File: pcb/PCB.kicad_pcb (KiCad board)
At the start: 4 copper layers, 82.4 x 100 mm, 140 parts, among them J1 DTM1312PA12PBR008, J2 TC2030, J3 Conn_02x08_Top_Bottom, Q1 Si4162DY, Q2 Si4162DY, Q3 Si4162DY, Q4 Si4162DY, Q5 Si4162DY, Q6 Si4162DY, U1 SN65HVD230, U10 MCP1416, U11 BTS7004-1EPP, U12 BTS7004-1EPP, U13 BTS7004-1EPP, U14 BTS7004-1EPP, U15 BTS7004-1EPP, U2 AMS1117-3.3, U3 STM32F103C8T6, U4 BTS7004-1EPP, U5 MCP1416, U6 MCP1416, U7 MCP1416, U8 MCP1416, U9 MCP1416, Y1 8MHz

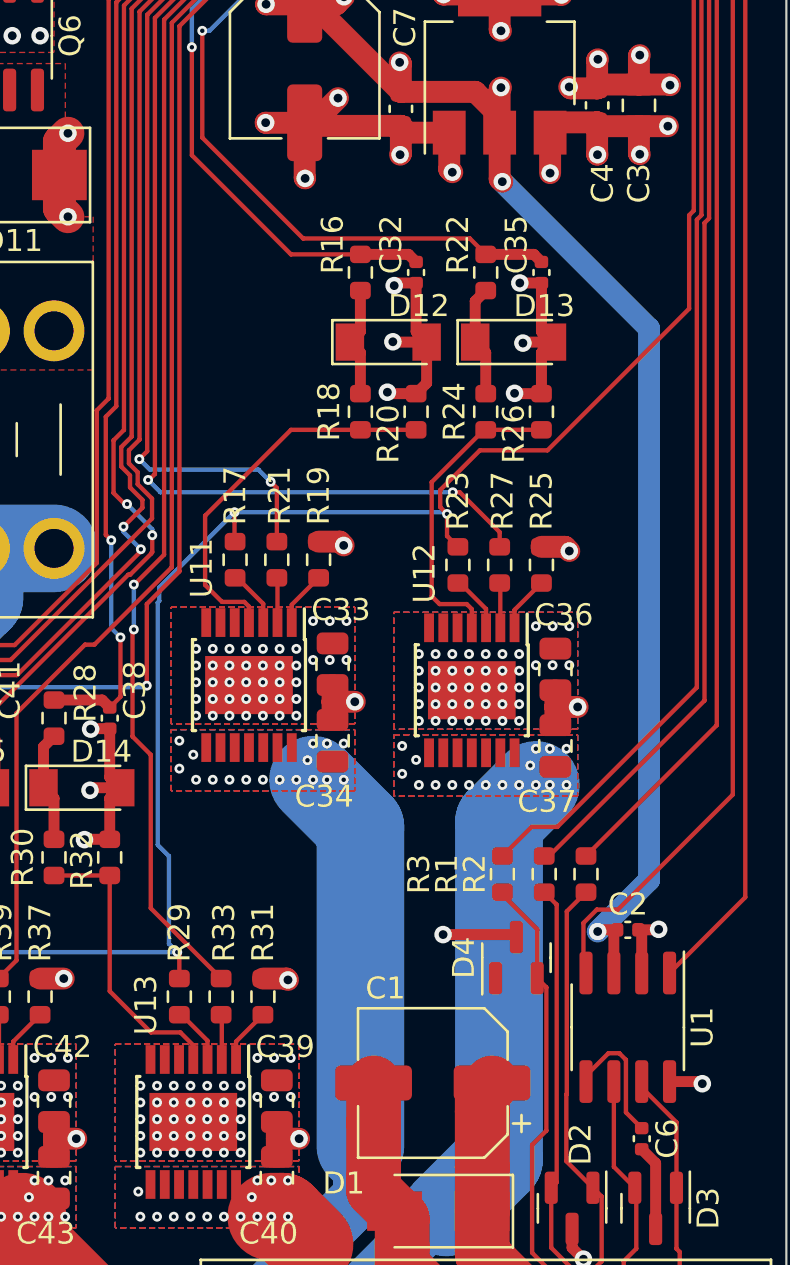
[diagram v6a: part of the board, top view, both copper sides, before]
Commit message: Added debug/test header
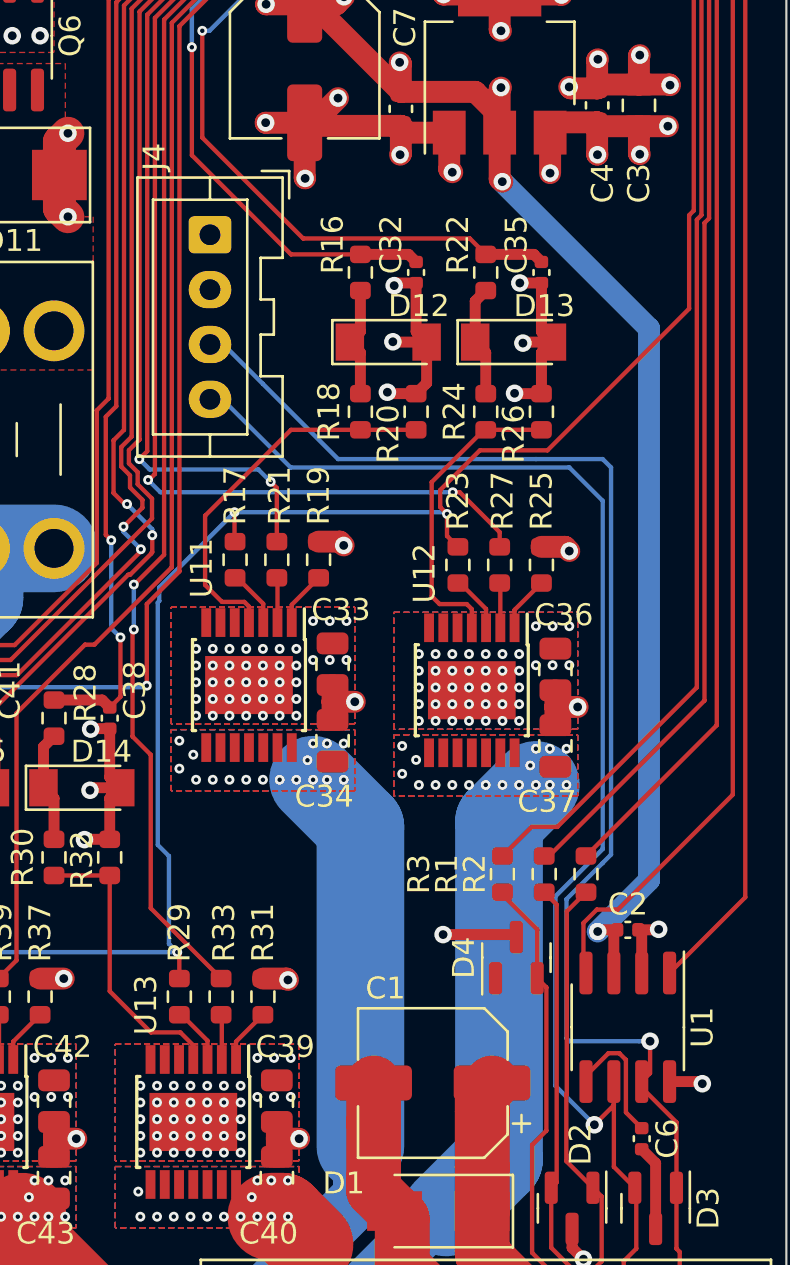
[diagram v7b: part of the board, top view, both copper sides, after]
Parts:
- added J4: JST B04B-XASK, Connector_JST:JST_XA_B04B-XASK-1_1x04_P2.50mm_Vertical, F.Cu at (124.0, 85.9)
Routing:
- net CAN+: track 11.3 -> 64.8 mm, vias 0 -> 1
- net CAN-: track 10.7 -> 63.2 mm, vias 0 -> 1
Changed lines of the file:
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@@
     )
   )
+  (footprint "Connector_JST:JST_XA_B04B-XASK-1_1x04_P2.50mm_Vertical" (layer "F.Cu")
+    (at 123.952 85.912 -90)
+    (descr "JST XA series connector, B04B-XASK-1 (http://www.jst-mfg.com/product/pdf/eng/eXA1.pdf), generated with kicad-footprint-generator")
+    (tags "connector JST XA vertical")
+    (property "Sheetfile" "File: PCB.kicad_sch")
+    (property "Sheetname" "")
+    (attr through_hole)
+    (fp_text reference "J4" (at -3.556 2.54 90) (layer "F.SilkS")
+      (effects (font (size 1 1) (thickness 0.15)))
+    )
+    (fp_text value "JST B04B-XASK" (at 3.75 4.4 90) (layer "F.Fab")
+      (effects (font (size 1 1) (thickness 0.15)))
+    )
+    (fp_text user "${REFERENCE}" (at 3.75 1.5 90) (layer "F.Fab")
+      (effects (font (size 1 1) (thickness 0.15)))
+    )
+    (fp_line (start 9.1 2.6) (end 9.1 -1.7) (layer "F.SilkS") (width 0.12))
+    (fp_line (start 2.95 -2.91) (end 2.95 -2.31) (layer "F.SilkS") (width 0.12))
+    (fp_line (start 10.11 3.31) (end 10.11 -3.31) (layer "F.SilkS") (width 0.12))
+    (fp_line (start -2.61 3.31) (end 10.11 3.31) (layer "F.SilkS") (width 0.12))
+    (fp_line (start -1.6 2.6) (end 9.1 2.6) (layer "F.SilkS") (width 0.12))
+    (fp_line (start 9.1 -1.7) (end -1.6 -1.7) (layer "F.SilkS") (width 0.12))
+    (fp_line (start -1.66 -3.61) (end -2.91 -3.61) (layer "F.SilkS") (width 0.12))
+    (fp_line (start 4.55 -2.31) (end 4.55 -2.91) (layer "F.SilkS") (width 0.12))
+    (fp_line (start 10.11 -3.31) (end 6.45 -3.31) (layer "F.SilkS") (width 0.12))
+    (fp_line (start -2.91 -3.61) (end -2.91 -2.36) (layer "F.SilkS") (width 0.12))
+    (fp_line (start 2.95 -2.31) (end 1.05 -2.31) (layer "F.SilkS") (width 0.12))
+    (fp_line (start -2.61 -3.31) (end -2.61 3.31) (layer "F.SilkS") (width 0.12))
+    (fp_line (start 1.05 -3.31) (end -2.61 -3.31) (layer "F.SilkS") (width 0.12))
+    (fp_line (start -1.6 -1.7) (end -1.6 2.6) (layer "F.SilkS") (width 0.12))
+    (fp_line (start 6.45 -2.31) (end 4.55 -2.31) (layer "F.SilkS") (width 0.12))
+    (fp_line (start 4.55 -2.91) (end 2.95 -2.91) (layer "F.SilkS") (width 0.12))
+    (fp_line (start 1.05 -2.31) (end 1.05 -3.31) (layer "F.SilkS") (width 0.12))
+    (fp_line (start 6.45 -3.31) (end 6.45 -2.31) (layer "F.SilkS") (width 0.12))
+    (fp_line (start 10.11 0) (end 9.1 0) (layer "F.SilkS") (width 0.12))
+    (fp_line (start -2.61 0) (end -1.6 0) (layer "F.SilkS") (width 0.12))
+    (fp_line (start 10.5 3.7) (end 10.5 -3.7) (layer "F.CrtYd") (width 0.05))
+    (fp_line (start -3 3.7) (end 10.5 3.7) (layer "F.CrtYd") (width 0.05))
+    (fp_line (start 10.5 -3.7) (end -3 -3.7) (layer "F.CrtYd") (width 0.05))
+    (fp_line (start -3 -3.7) (end -3 3.7) (layer "F.CrtYd") (width 0.05))
+    (fp_line (start -2.91 -3.61) (end -2.91 -2.36) (layer "F.Fab") (width 0.1))
+    (fp_line (start 10 -3.2) (end -2.5 -3.2) (layer "F.Fab") (width 0.1))
+    (fp_line (start 10 3.2) (end 10 -3.2) (layer "F.Fab") (width 0.1))
+    (fp_line (start -1.66 -3.61) (end -2.91 -3.61) (layer "F.Fab") (width 0.1))
+    (fp_line (start -2.5 3.2) (end 10 3.2) (layer "F.Fab") (width 0.1))
+    (fp_line (start -2.5 -3.2) (end -2.5 3.2) (layer "F.Fab") (width 0.1))
+    (pad "1" thru_hole roundrect (at 0 0 270) (size 1.7 1.95) (drill 0.95) (layers *.Cu *.Mask) (roundrect_rratio 0.147059)
+      (net 3 "+12V") (pinfunction "Pin_1") (pintype "passive"))
+    (pad "2" thru_hole oval (at 2.5 0 270) (size 1.7 1.95) (drill 0.95) (layers *.Cu *.Mask)
+      (net 1 "GND") (pinfunction "Pin_2") (pintype "passive"))
+    (pad "3" thru_hole oval (at 5 0 270) (size 1.7 1.95) (drill 0.95) (layers *.Cu *.Mask)
+      (net 26 "CAN+") (pinfunction "Pin_3") (pintype "passive"))
+    (pad "4" thru_hole oval (at 7.5 0 270) (size 1.7 1.95) (drill 0.95) (layers *.Cu *.Mask)
+      (net 27 "CAN-") (pinfunction "Pin_4") (pintype "passive"))
+    (model "${KICAD6_3DMODEL_DIR}/Connector_JST.3dshapes/JST_XA_B04B-XASK-1_1x04_P2.50mm_Vertical.wrl"
+      (offset (xyz 0 0 0))
+      (scale (xyz 1 1 1))
+      (rotate (xyz 0 0 0))
+    )
+  )
   (footprint "Crystal:Crystal_SMD_5032-2Pin_5.0x3.2mm" (layer "F.Cu")
     (at 128.524 50.8 180)
@@
   (segment (start 139.76 129.1165) (end 139.512 129.3645) (width 0.2) (layer "F.Cu") (net 25))
   (segment (start 139.512 132.102) (end 139.512 129.3645) (width 0.2) (layer "F.Cu") (net 25))
+  (segment (start 144.018 122.682) (end 144.018 124.141) (width 0.2) (layer "F.Cu") (net 26))
   (segment (start 145.222 129.3645) (end 145.222 132.142) (width 0.2) (layer "F.Cu") (net 26))
   (segment (start 145.222 126.377685) (end 143.637 124.792685) (width 0.2) (layer "F.Cu") (net 26))
+  (segment (start 144.018 124.141) (end 143.637 124.522) (width 0.2) (layer "F.Cu") (net 26))
   (segment (start 145.222 129.3645) (end 145.222 126.377685) (width 0.2) (layer "F.Cu") (net 26))
   (segment (start 145.222 132.142) (end 145.37 132.29) (width 0.2) (layer "F.Cu") (net 26))
   (segment (start 145.37 133.015) (end 147.007 134.652) (width 0.2) (layer "F.Cu") (net 26))
   (segment (start 145.37 132.29) (end 145.37 133.015) (width 0.2) (layer "F.Cu") (net 26))
+  (via (at 144.018 122.682) (size 0.8) (drill 0.4) (layers "F.Cu" "B.Cu") (net 26))
+  (segment (start 143.51 122.682) (end 144.018 122.682) (width 0.2) (layer "B.Cu") (net 26))
+  (segment (start 140.208 122.555) (end 140.335 122.682) (width 0.2) (layer "B.Cu") (net 26))
+  (segment (start 141.859 96.139) (end 142.24 96.52) (width 0.2) (layer "B.Cu") (net 26))
+  (segment (start 123.952 90.344) (end 123.999 90.344) (width 0.2) (layer "B.Cu") (net 26))
+  (segment (start 138.811 96.139) (end 141.859 96.139) (width 0.2) (layer "B.Cu") (net 26))
+  (segment (start 141.859 114.554) (end 140.208 116.205) (width 0.2) (layer "B.Cu") (net 26))
+  (segment (start 126.365 92.71) (end 129.794 96.139) (width 0.2) (layer "B.Cu") (net 26))
+  (segment (start 142.24 96.52) (end 142.24 114.173) (width 0.2) (layer "B.Cu") (net 26))
+  (segment (start 140.208 116.205) (end 140.208 122.555) (width 0.2) (layer "B.Cu") (net 26))
+  (segment (start 142.24 114.173) (end 141.859 114.554) (width 0.2) (layer "B.Cu") (net 26))
+  (segment (start 129.794 96.139) (end 138.811 96.139) (width 0.2) (layer "B.Cu") (net 26))
+  (segment (start 123.999 90.344) (end 126.365 92.71) (width 0.2) (layer "B.Cu") (net 26))
+  (segment (start 140.335 122.682) (end 143.51 122.682) (width 0.2) (layer "B.Cu") (net 26))
   (segment (start 143.39 132.14) (end 142.817 132.713) (width 0.2) (layer "F.Cu") (net 27))
   (segment (start 143.39 129.4325) (end 143.39 132.14) (width 0.2) (layer "F.Cu") (net 27))
   (segment (start 143.322 129.3645) (end 142.367 128.4095) (width 0.2) (layer "F.Cu") (net 27))
   (segment (start 142.367 128.4095) (end 142.367 124.522) (width 0.2) (layer "F.Cu") (net 27))
+  (segment (start 142.367 124.522) (end 142.367 125.603) (width 0.2) (layer "F.Cu") (net 27))
+  (segment (start 142.367 125.603) (end 141.478 126.492) (width 0.2) (layer "F.Cu") (net 27))
   (segment (start 142.817 132.713) (end 142.817 134.652) (width 0.2) (layer "F.Cu") (net 27))
+  (via (at 141.478 126.492) (size 0.8) (drill 0.4) (layers "F.Cu" "B.Cu") (net 27))
+  (segment (start 141.859 113.919) (end 139.7 116.078) (width 0.2) (layer "B.Cu") (net 27))
+  (segment (start 140.335 96.52) (end 141.859 98.044) (width 0.2) (layer "B.Cu") (net 27))
+  (segment (start 141.859 98.044) (end 141.859 113.919) (width 0.2) (layer "B.Cu") (net 27))
+  (segment (start 127.628 96.52) (end 140.335 96.52) (width 0.2) (layer "B.Cu") (net 27))
+  (segment (start 139.7 116.078) (end 139.7 124.714) (width 0.2) (layer "B.Cu") (net 27))
+  (segment (start 139.7 124.714) (end 141.478 126.492) (width 0.2) (layer "B.Cu") (net 27))
+  (segment (start 123.952 92.844) (end 127.628 96.52) (width 0.2) (layer "B.Cu") (net 27))
   (segment (start 130.81 91.285) (end 130.33 90.805) (width 0.5) (layer "F.Cu") (net 33))
   (segment (start 130.81 93.155) (end 130.81 91.285) (width 0.5) (layer "F.Cu") (net 33))

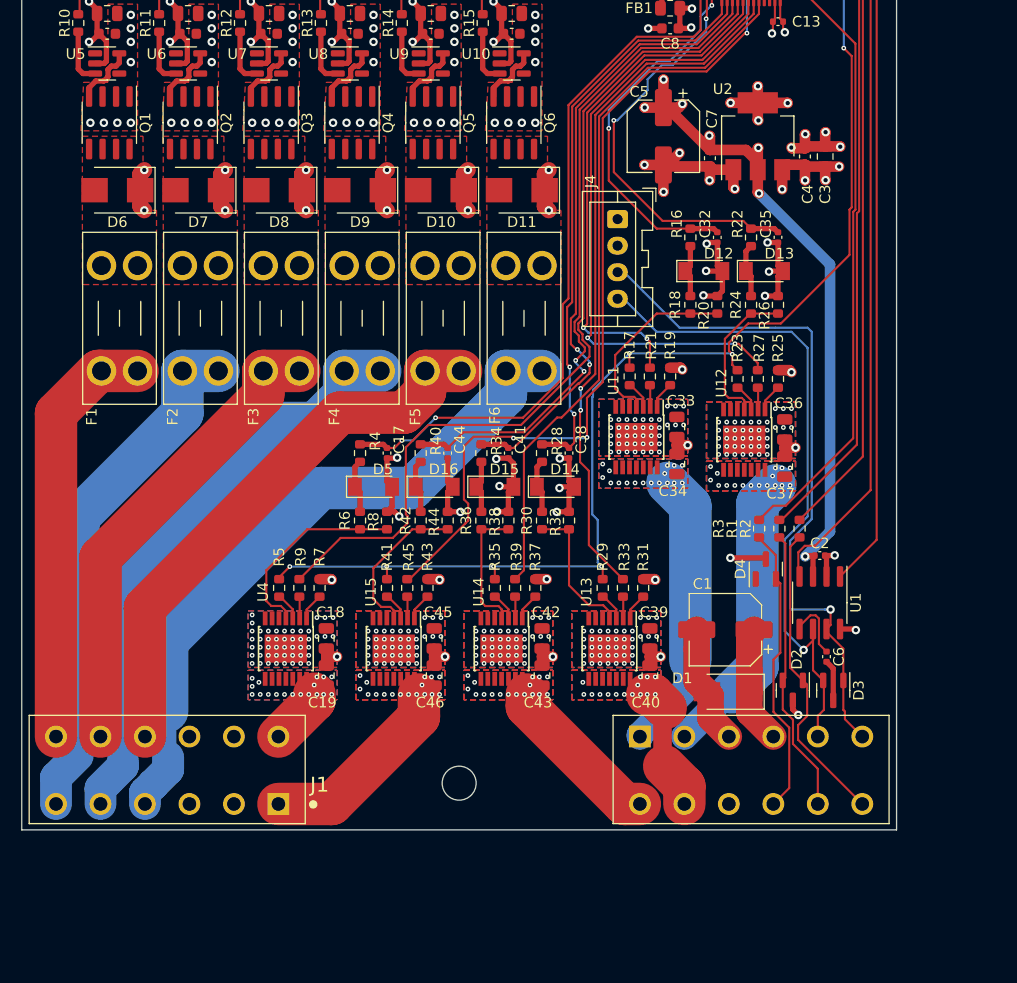
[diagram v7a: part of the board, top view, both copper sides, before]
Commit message: Switched to non-sketchy regulator
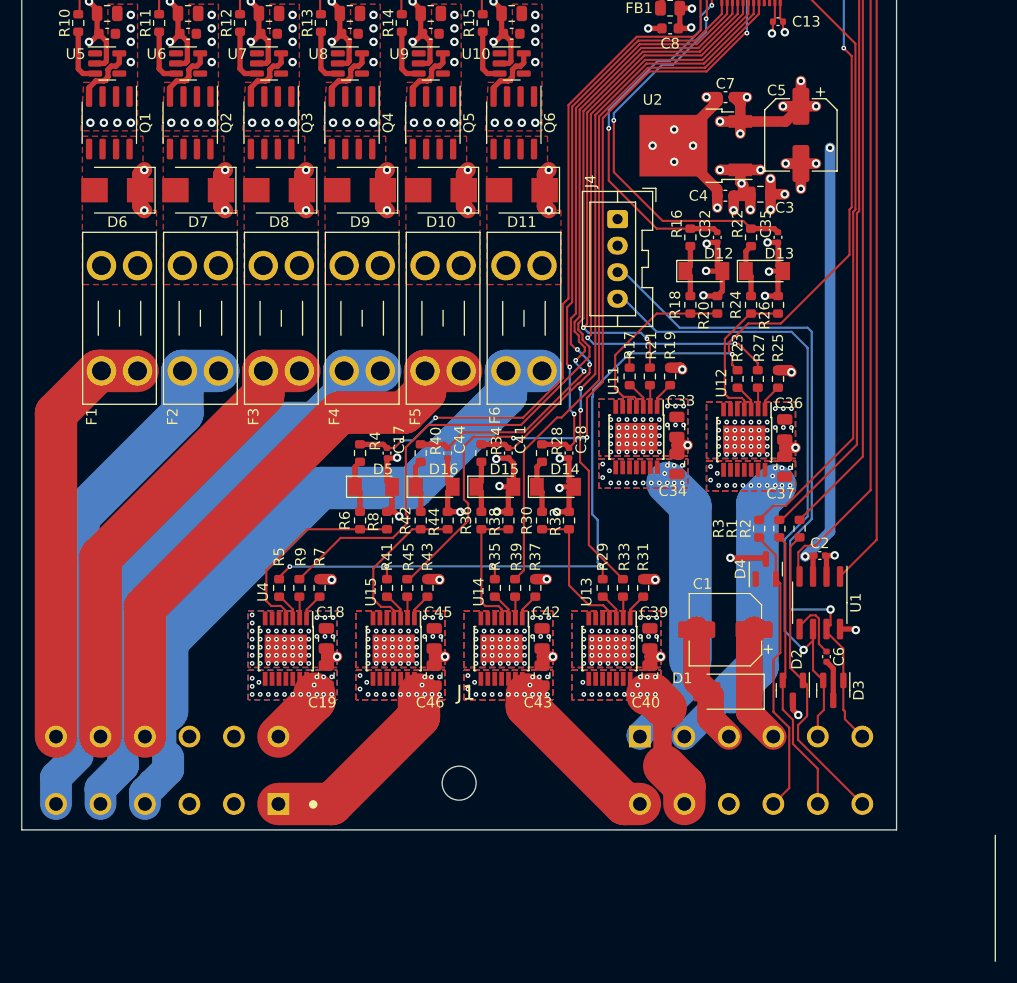
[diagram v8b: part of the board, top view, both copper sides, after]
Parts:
- U2: value AMS1117-3.3 -> LF33_TO252; footprint Package_TO_SOT_SMD:SOT-223-3_TabPin2 -> Package_TO_SOT_SMD:TO-252-2
- moved C5 13.0 mm to (141.2, 78.0)
- moved C4 8.36 mm to (134.1, 83.7), turned to 180 degrees
- moved C3 7.06 mm to (137.4, 83.6), turned to 0 degrees
- moved C7 5.93 mm to (134.1, 74.4), turned to 180 degrees
- moved U2 5.91 mm to (131.3, 79.0), turned to 180 degrees
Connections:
- U2 pad 1: GND -> +12V
- U2 pad 2: +3V3 -> GND
- U2 pad 3: +12V -> +3V3
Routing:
- net +3V3: track 95.6 -> 83.3 mm, vias 19 -> 16
- net GND: track 145.0 -> 152.7 mm, vias 98 -> 101
- net +12V: track 94.9 -> 95.4 mm, vias 281 -> 282
